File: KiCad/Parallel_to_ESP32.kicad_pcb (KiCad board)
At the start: 2 copper layers, 47 x 50 mm, 21 parts, among them J1 DB25_Male, J2 Micro_SD_Card_Socket, J3 Conn_01x02, J4 Conn_01x02, U1 ESP32-DEVKIT-V1, U2 SN74CB3T16210

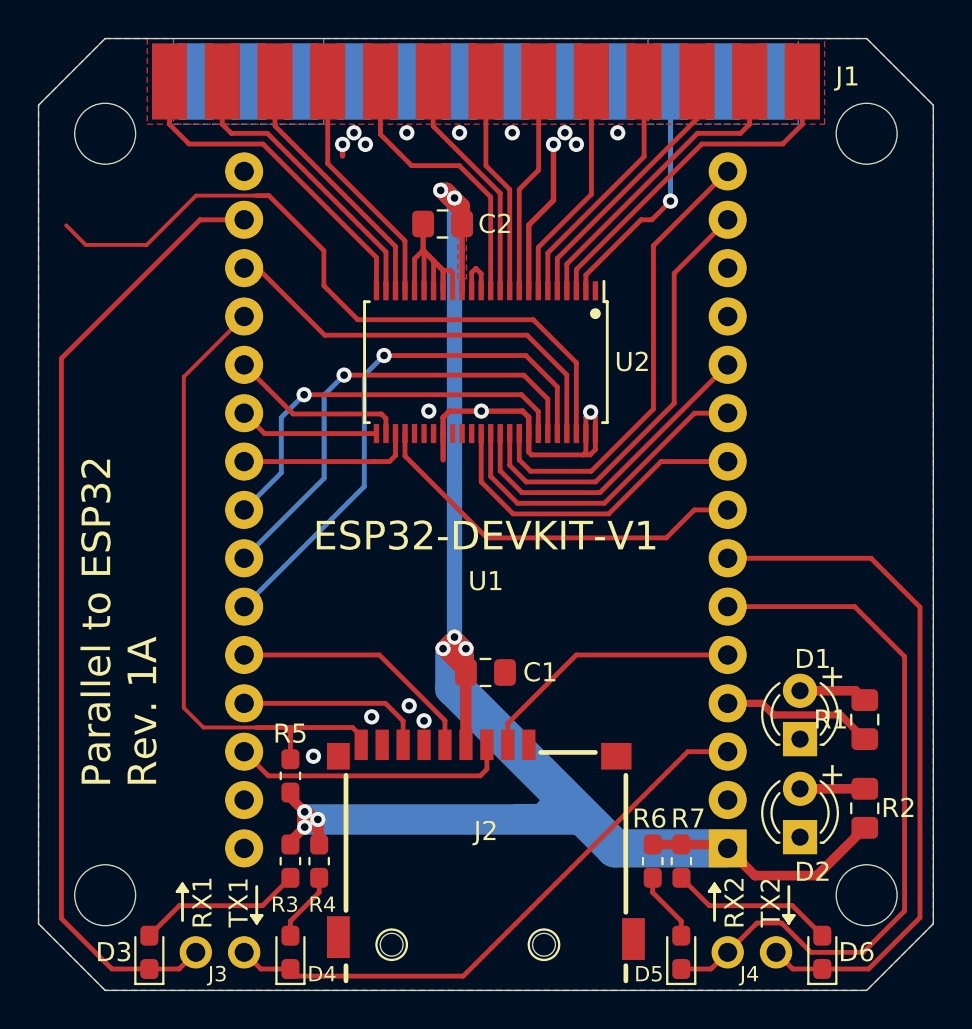
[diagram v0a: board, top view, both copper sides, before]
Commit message: Added jumper JP1 for RESET-signal (optional)
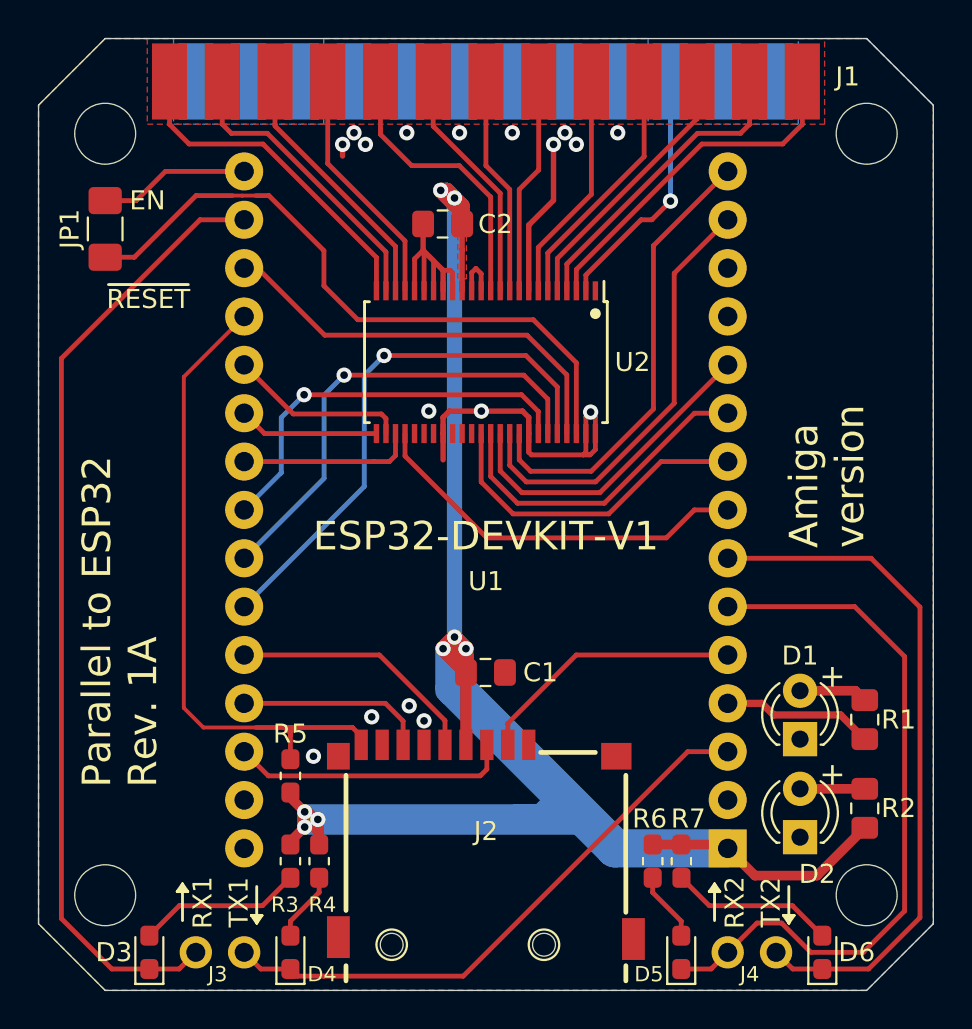
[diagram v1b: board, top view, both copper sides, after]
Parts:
- added JP1: Jumper_2_Open, Resistor_SMD:R_1206_3216Metric_Pad1.42x1.75mm_HandSolder, F.Cu at (127.7, 95.0)
- R1, R2: value 200 -> 150
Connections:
- U1 pad 16: Net-(U1-Pad16) -> EN
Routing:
- net EN: track 0.00 -> 7.93 mm
- net RESET_3V3: track 36.7 -> 34.5 mm
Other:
- board text added: "Amiga version"
- board text added: "EN"
- board text added: "~RESET"

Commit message: Changed to surface mount footprint for UART1 and UART2 and 3V3/GND on underside, changed JP1 to regular PinHeader P2.54mm
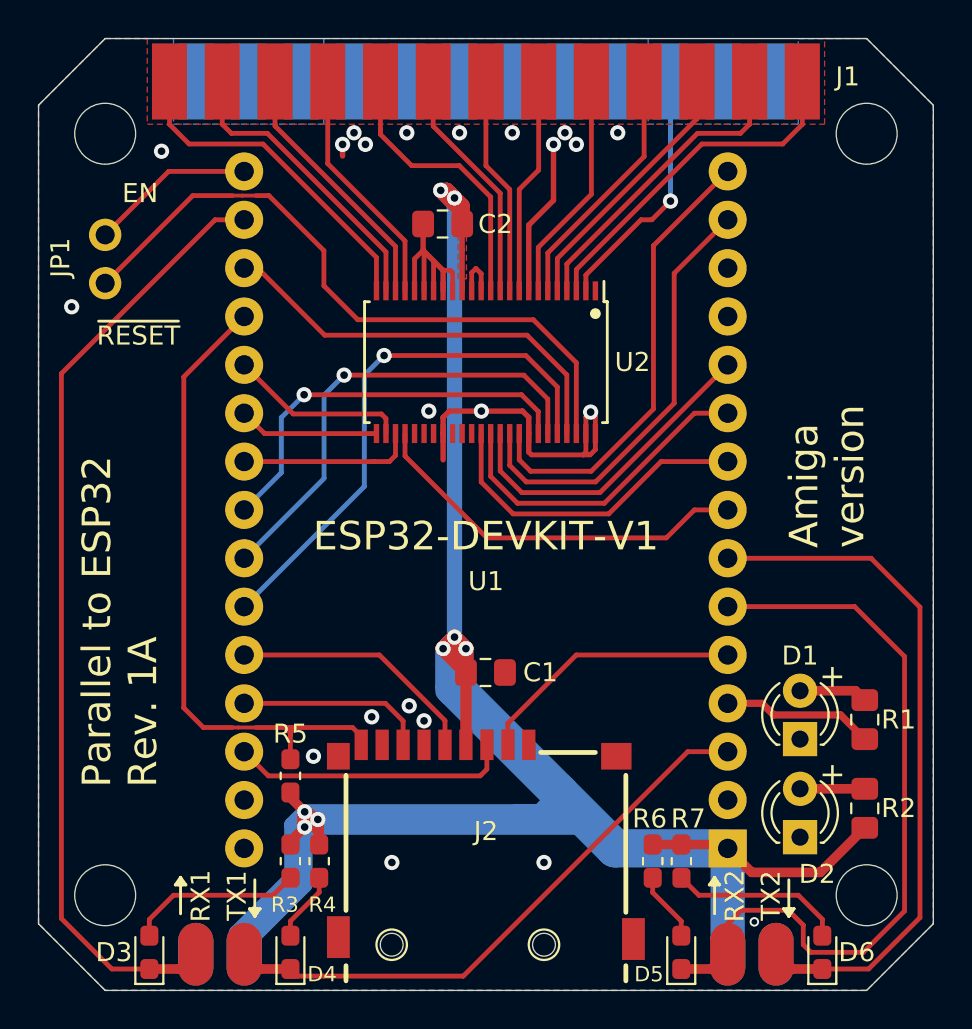
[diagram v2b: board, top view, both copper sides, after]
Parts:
- J3, J4: value Conn_01x02 -> Conn_02x02_Top_Bottom; footprint Connector_PinHeader_2.54mm:PinHeader_1x02_P2.54mm_Vertical -> Parallel_to_ESP32:PinHeader_2x02_P2.54mm_EdgeMount_SMD
- JP1: footprint Resistor_SMD:R_1206_3216Metric_Pad1.42x1.75mm_HandSolder -> Connector_PinHeader_2.54mm:PinHeader_1x02_P2.54mm_Vertical
- moved J3 1.27 mm to (133.7, 133.0), turned to 0 degrees
- moved J4 1.27 mm to (161.7, 133.0), turned to 0 degrees
- moved JP1 0.31 mm to (127.7, 95.3), turned to 0 degrees
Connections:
- J3 pad 1: TX1 -> RX1
- J3 pad 2: RX1 -> TX1
- J4 pad 1: TX2 -> RX2
- J4 pad 2: RX2 -> TX2
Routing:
- net 3V3: track 140.2 -> 178.2 mm
- net RX2: track 38.0 -> 40.1 mm
- net EN: track 7.93 -> 8.68 mm
- net TX1: track 31.4 -> 30.8 mm
- net RESET_3V3: track 34.5 -> 35.1 mm
- net Net-(D3-Pad2): track 8.67 -> 9.17 mm
- net GND: vias 17 -> 22
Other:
- board text added: "3V3"
- board text added: "GND"

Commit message: Added optional pull-up resistor packs for all Parallel-port-signals pulled up by Amigas 5V (pin 14)
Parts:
- added C3: 0.1uF, Capacitor_SMD:C_0805_2012Metric_Pad1.15x1.40mm_HandSolder, B.Cu at (157.3, 98.4)
- added C4: 0.1uF, Capacitor_SMD:C_0805_2012Metric_Pad1.15x1.40mm_HandSolder, B.Cu at (139.1, 97.2)
- added R8: 10k, Resistor_SMD:R_0603_1608Metric_Pad1.05x0.95mm_HandSolder, B.Cu at (164.1, 91.8)
- added RN1: 10k_R_Pack04, Parallel_to_ESP32:RESCAF80P320X160X60-8N, B.Cu at (154.4, 94.6)
- added RN2: 10k_R_Pack04, Parallel_to_ESP32:RESCAF80P320X160X60-8N, B.Cu at (149.2, 98.7)
- added RN3: 10k_R_Pack04, Parallel_to_ESP32:RESCAF80P320X160X60-8N, B.Cu at (142.2, 93.9)
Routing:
- net Amiga_5V: track 0.00 -> 69.6 mm, vias 0 -> 6
- net GND: track 40.6 -> 29.6 mm, vias 22 -> 33
- net D4: track 11.4 -> 15.6 mm, vias 0 -> 1
- net D5: track 11.5 -> 15.2 mm, vias 0 -> 1
- net D0: track 16.3 -> 18.9 mm, vias 0 -> 1
- net D6: track 12.5 -> 15.1 mm, vias 0 -> 1
- net STROBE: track 18.4 -> 20.7 mm, vias 0 -> 1
- net D1: track 14.0 -> 16.0 mm, vias 0 -> 1
- net POUT: track 15.7 -> 17.6 mm, vias 0 -> 1
- net ACK: track 12.7 -> 14.6 mm, vias 0 -> 1
- net D2: track 13.1 -> 14.9 mm, vias 0 -> 1
- net D7: track 14.9 -> 16.6 mm, vias 0 -> 1
- net BUSY: track 13.6 -> 14.7 mm, vias 0 -> 1
- net SELECT: track 17.8 -> 18.8 mm, vias 0 -> 1
- net D3: track 12.2 -> 13.2 mm, vias 0 -> 1
- removed copper zone on F.Cu, net 3V3
